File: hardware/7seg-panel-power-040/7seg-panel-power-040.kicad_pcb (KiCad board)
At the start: 2 copper layers, 81.3 x 33 mm, 25 parts, among them J101 VBUS GND, J102 USB_C_Receptacle_PowerOnly_6P, J103 +5V GND, J104 VBUS GND, U101 K7805M-2000, U103 CH221K

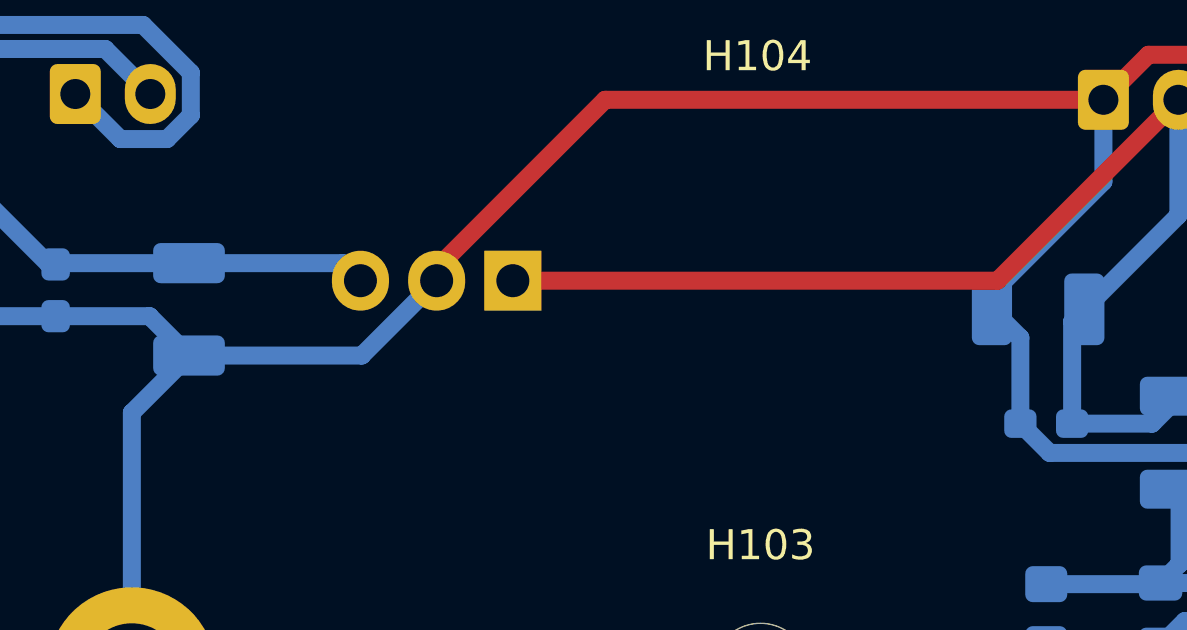
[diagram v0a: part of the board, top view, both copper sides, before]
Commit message: ファイル再生時の音声と動画の同期確認
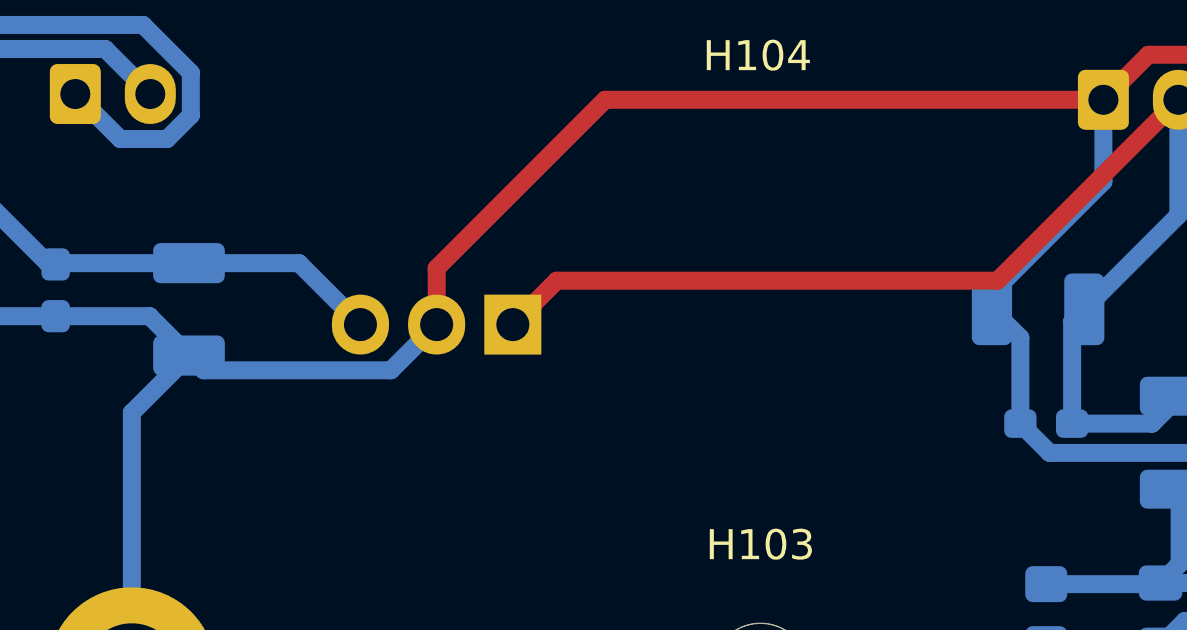
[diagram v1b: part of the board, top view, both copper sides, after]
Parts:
- moved U101 1.46 mm to (134.5, 124.3)
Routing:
- net GND: track 164.1 -> 165.4 mm
- net VBUS: track 56.2 -> 56.8 mm
- net +5V: track 29.5 -> 30.1 mm
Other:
- board text added: "<<DIGITI>> Power 040 2026-03-06 Hijiri Umemoto"
- board text removed: "<<DIGITI>> 040 1d Power 2026-02-22 Hijiri Umemoto"
